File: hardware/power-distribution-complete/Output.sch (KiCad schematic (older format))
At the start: 88 parts, among them J18 POUT, J19 POUT, J20 POUT, J21 POUT, J22 POUT, J23 POUT, J24 POUT, J25 POUT, J26 POUT, J27 POUT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

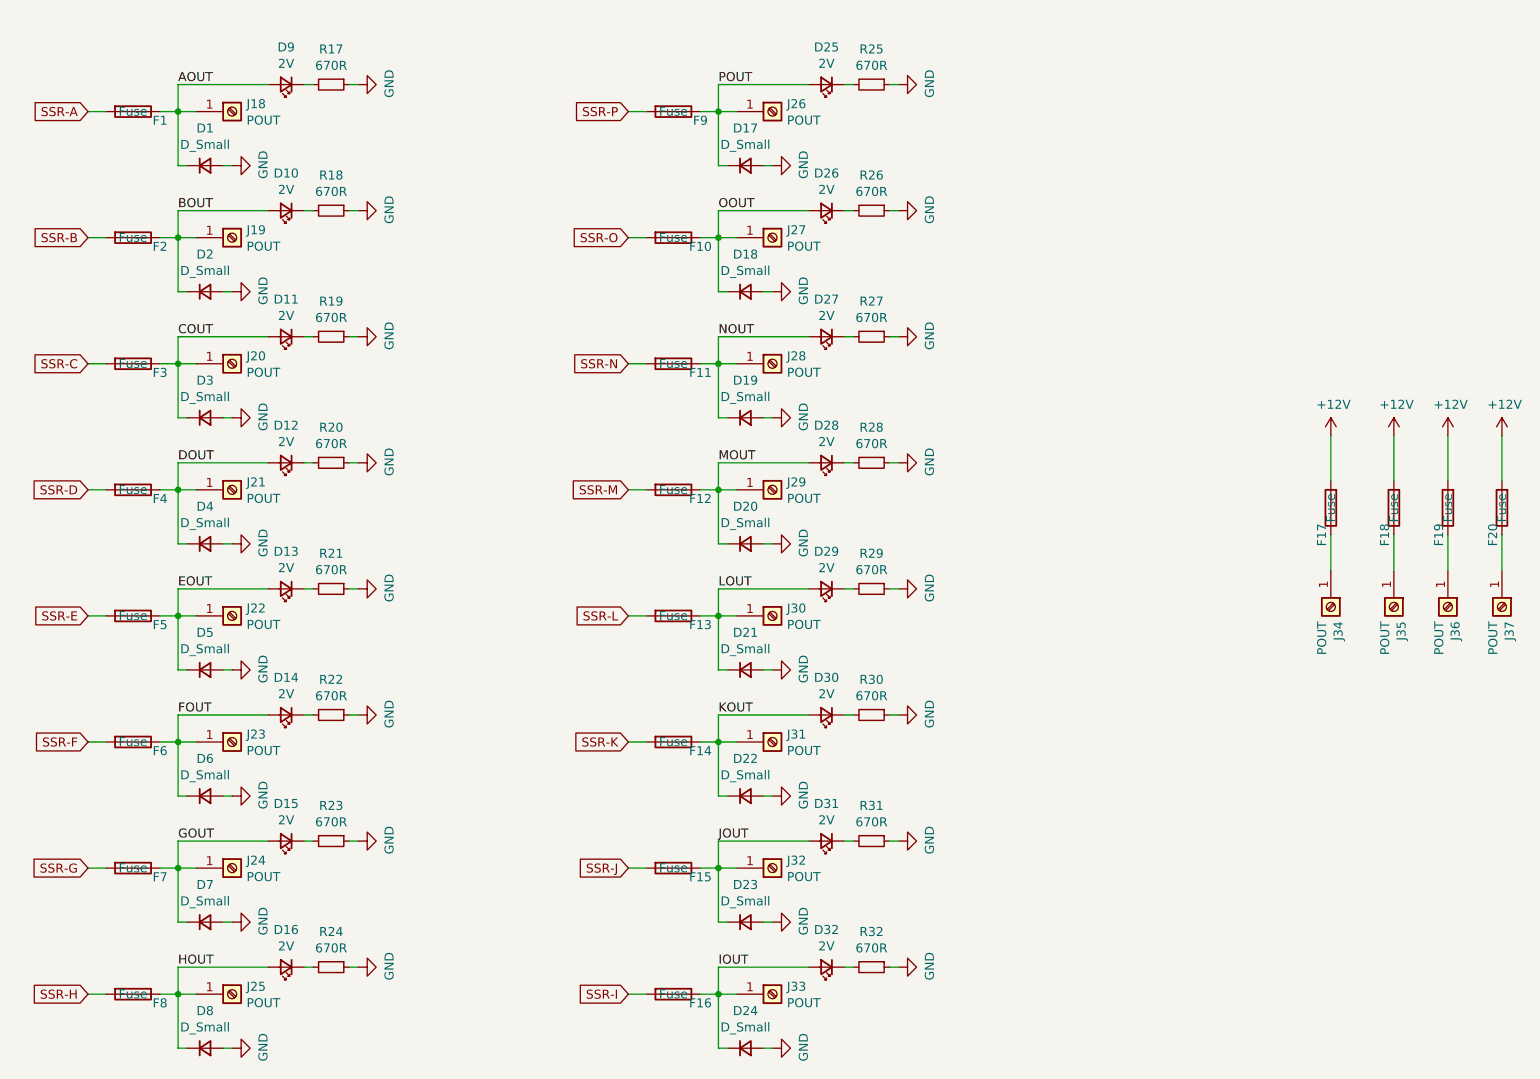
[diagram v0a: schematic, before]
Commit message: Updated the power distribution schematic and pcb
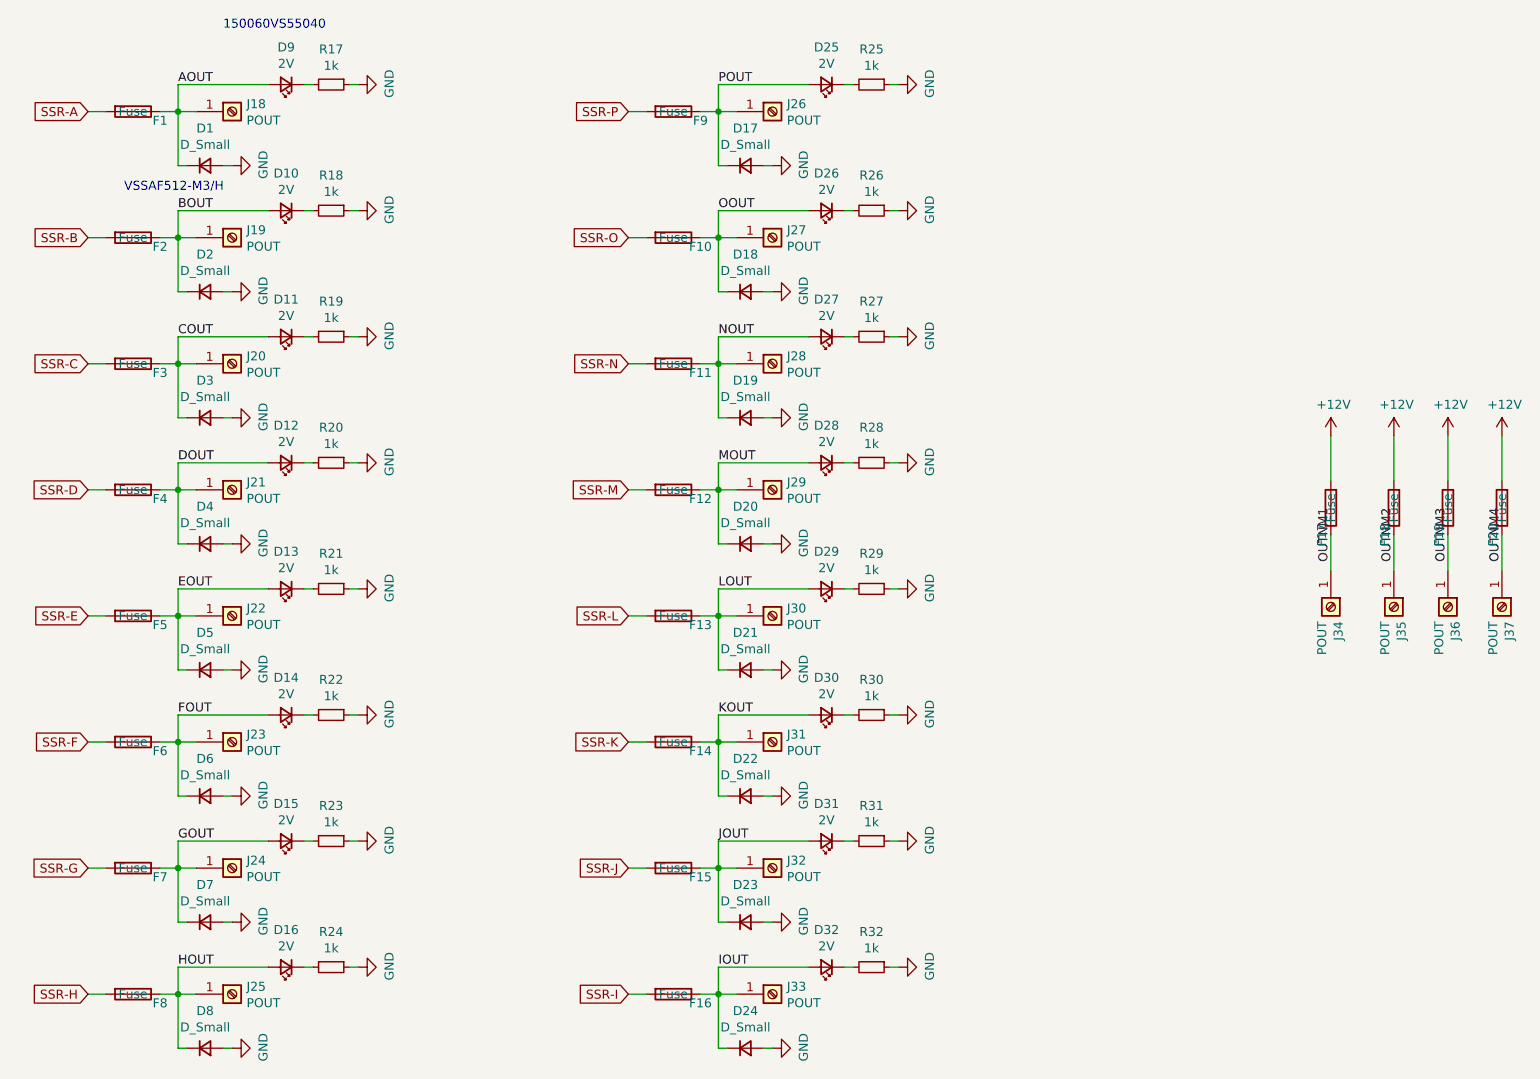
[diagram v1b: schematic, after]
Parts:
- D1, D17, D18, D19, D2, D20, D21, D22, D23, D24, D3, D4, D5, D6, D7, D8: footprint (none) -> diode:SlimSMA_DO-221AC-2
- R17, R18, R19, R20, R21, R22, R23, R24, R25, R26, R27, R28, R29, R30, R31, R32: value 670R -> 1k
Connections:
- net OUTNM1: now reaches F17.1, J34.1 (Pin_1)
- net OUTNM2: now reaches F18.1, J35.1 (Pin_1)
- net OUTNM3: now reaches F19.1, J36.1 (Pin_1)
- net OUTNM4: now reaches F20.1, J37.1 (Pin_1)
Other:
- note added: "150060VS55040"
- note added: "VSSAF512-M3/H"
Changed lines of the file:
@@
 AR Path="/5FEC946E/5FED2B12" Ref="R17"  Part="1"
 F 0 "R17" V 2654 1450 50  0000 C CNN
-F 1 "670R" V 2745 1450 50  0000 C CNN
+F 1 "1k" V 2745 1450 50  0000 C CNN
 F 2 "Resistor_SMD:R_0603_1608Metric" H 2850 1450 50  0001 C CNN
 F 3 "~" H 2850 1450 50  0001 C CNN
@@
 AR Path="/5FEC946E/5FED2B27" Ref="R18"  Part="1"
 F 0 "R18" V 2654 2150 50  0000 C CNN
-F 1 "670R" V 2745 2150 50  0000 C CNN
+F 1 "1k" V 2745 2150 50  0000 C CNN
 F 2 "Resistor_SMD:R_0603_1608Metric" H 2850 2150 50  0001 C CNN
 F 3 "~" H 2850 2150 50  0001 C CNN
@@
 AR Path="/5FEC946E/5FED2B3B" Ref="R19"  Part="1"
 F 0 "R19" V 2654 2850 50  0000 C CNN
-F 1 "670R" V 2745 2850 50  0000 C CNN
+F 1 "1k" V 2745 2850 50  0000 C CNN
 F 2 "Resistor_SMD:R_0603_1608Metric" H 2850 2850 50  0001 C CNN
 F 3 "~" H 2850 2850 50  0001 C CNN
@@
 AR Path="/5FEC946E/5FED2B4F" Ref="R20"  Part="1"
 F 0 "R20" V 2654 3550 50  0000 C CNN
-F 1 "670R" V 2745 3550 50  0000 C CNN
+F 1 "1k" V 2745 3550 50  0000 C CNN
 F 2 "Resistor_SMD:R_0603_1608Metric" H 2850 3550 50  0001 C CNN
 F 3 "~" H 2850 3550 50  0001 C CNN
@@
 AR Path="/5FEC946E/5FEE4BC2" Ref="R21"  Part="1"
 F 0 "R21" V 2654 4250 50  0000 C CNN
-F 1 "670R" V 2745 4250 50  0000 C CNN
+F 1 "1k" V 2745 4250 50  0000 C CNN
 F 2 "Resistor_SMD:R_0603_1608Metric" H 2850 4250 50  0001 C CNN
 F 3 "~" H 2850 4250 50  0001 C CNN
@@
 AR Path="/5FEC946E/5FEE4BD7" Ref="R22"  Part="1"
 F 0 "R22" V 2654 4950 50  0000 C CNN
-F 1 "670R" V 2745 4950 50  0000 C CNN
+F 1 "1k" V 2745 4950 50  0000 C CNN
 F 2 "Resistor_SMD:R_0603_1608Metric" H 2850 4950 50  0001 C CNN
 F 3 "~" H 2850 4950 50  0001 C CNN
@@
 AR Path="/5FEC946E/5FEE4BEB" Ref="R23"  Part="1"
 F 0 "R23" V 2654 5650 50  0000 C CNN
-F 1 "670R" V 2745 5650 50  0000 C CNN
+F 1 "1k" V 2745 5650 50  0000 C CNN
 F 2 "Resistor_SMD:R_0603_1608Metric" H 2850 5650 50  0001 C CNN
 F 3 "~" H 2850 5650 50  0001 C CNN
@@
 AR Path="/5FEC946E/5FEE4BFF" Ref="R24"  Part="1"
 F 0 "R24" V 2654 6350 50  0000 C CNN
-F 1 "670R" V 2745 6350 50  0000 C CNN
+F 1 "1k" V 2745 6350 50  0000 C CNN
 F 2 "Resistor_SMD:R_0603_1608Metric" H 2850 6350 50  0001 C CNN
 F 3 "~" H 2850 6350 50  0001 C CNN
@@
 AR Path="/5FEC946E/5FF051C6" Ref="R25"  Part="1"
 F 0 "R25" V 5654 1450 50  0000 C CNN
-F 1 "670R" V 5745 1450 50  0000 C CNN
+F 1 "1k" V 5745 1450 50  0000 C CNN
 F 2 "Resistor_SMD:R_0603_1608Metric" H 5850 1450 50  0001 C CNN
 F 3 "~" H 5850 1450 50  0001 C CNN
@@
 AR Path="/5FEC946E/5FF051DB" Ref="R26"  Part="1"
 F 0 "R26" V 5654 2150 50  0000 C CNN
-F 1 "670R" V 5745 2150 50  0000 C CNN
+F 1 "1k" V 5745 2150 50  0000 C CNN
 F 2 "Resistor_SMD:R_0603_1608Metric" H 5850 2150 50  0001 C CNN
 F 3 "~" H 5850 2150 50  0001 C CNN
@@
 AR Path="/5FEC946E/5FF051EF" Ref="R27"  Part="1"
 F 0 "R27" V 5654 2850 50  0000 C CNN
-F 1 "670R" V 5745 2850 50  0000 C CNN
+F 1 "1k" V 5745 2850 50  0000 C CNN
 F 2 "Resistor_SMD:R_0603_1608Metric" H 5850 2850 50  0001 C CNN
 F 3 "~" H 5850 2850 50  0001 C CNN
@@
 AR Path="/5FEC946E/5FF05203" Ref="R28"  Part="1"
 F 0 "R28" V 5654 3550 50  0000 C CNN
-F 1 "670R" V 5745 3550 50  0000 C CNN
+F 1 "1k" V 5745 3550 50  0000 C CNN
 F 2 "Resistor_SMD:R_0603_1608Metric" H 5850 3550 50  0001 C CNN
 F 3 "~" H 5850 3550 50  0001 C CNN
@@
 AR Path="/5FEC946E/5FF05266" Ref="R29"  Part="1"
 F 0 "R29" V 5654 4250 50  0000 C CNN
-F 1 "670R" V 5745 4250 50  0000 C CNN
+F 1 "1k" V 5745 4250 50  0000 C CNN
 F 2 "Resistor_SMD:R_0603_1608Metric" H 5850 4250 50  0001 C CNN
 F 3 "~" H 5850 4250 50  0001 C CNN
@@
 AR Path="/5FEC946E/5FF0527B" Ref="R30"  Part="1"
 F 0 "R30" V 5654 4950 50  0000 C CNN
-F 1 "670R" V 5745 4950 50  0000 C CNN
+F 1 "1k" V 5745 4950 50  0000 C CNN
 F 2 "Resistor_SMD:R_0603_1608Metric" H 5850 4950 50  0001 C CNN
 F 3 "~" H 5850 4950 50  0001 C CNN
@@
 AR Path="/5FEC946E/5FF0528F" Ref="R31"  Part="1"
 F 0 "R31" V 5654 5650 50  0000 C CNN
-F 1 "670R" V 5745 5650 50  0000 C CNN
+F 1 "1k" V 5745 5650 50  0000 C CNN
 F 2 "Resistor_SMD:R_0603_1608Metric" H 5850 5650 50  0001 C CNN
 F 3 "~" H 5850 5650 50  0001 C CNN
@@
 AR Path="/5FEC946E/5FF052A3" Ref="R32"  Part="1"
 F 0 "R32" V 5654 6350 50  0000 C CNN
-F 1 "670R" V 5745 6350 50  0000 C CNN
+F 1 "1k" V 5745 6350 50  0000 C CNN
 F 2 "Resistor_SMD:R_0603_1608Metric" H 5850 6350 50  0001 C CNN
 F 3 "~" H 5850 6350 50  0001 C CNN
@@
 F 0 "D1" H 2150 2107 50  0000 C CNN
 F 1 "D_Small" H 2150 2016 50  0000 C CNN
-F 2 "" V 2150 1900 50  0001 C CNN
+F 2 "diode:SlimSMA_DO-221AC-2" V 2150 1900 50  0001 C CNN
 F 3 "~" V 2150 1900 50  0001 C CNN
 	1    2150 1900
@@
 F 0 "D2" H 2150 2807 50  0000 C CNN
 F 1 "D_Small" H 2150 2716 50  0000 C CNN
-F 2 "" V 2150 2600 50  0001 C CNN
+F 2 "diode:SlimSMA_DO-221AC-2" V 2150 2600 50  0001 C CNN
 F 3 "~" V 2150 2600 50  0001 C CNN
 	1    2150 2600
@@
 F 0 "D3" H 2150 3507 50  0000 C CNN
 F 1 "D_Small" H 2150 3416 50  0000 C CNN
-F 2 "" V 2150 3300 50  0001 C CNN
+F 2 "diode:SlimSMA_DO-221AC-2" V 2150 3300 50  0001 C CNN
 F 3 "~" V 2150 3300 50  0001 C CNN
 	1    2150 3300
@@
 F 0 "D4" H 2150 4207 50  0000 C CNN
 F 1 "D_Small" H 2150 4116 50  0000 C CNN
-F 2 "" V 2150 4000 50  0001 C CNN
+F 2 "diode:SlimSMA_DO-221AC-2" V 2150 4000 50  0001 C CNN
 F 3 "~" V 2150 4000 50  0001 C CNN
 	1    2150 4000
@@
 F 0 "D5" H 2150 4907 50  0000 C CNN
 F 1 "D_Small" H 2150 4816 50  0000 C CNN
-F 2 "" V 2150 4700 50  0001 C CNN
+F 2 "diode:SlimSMA_DO-221AC-2" V 2150 4700 50  0001 C CNN
 F 3 "~" V 2150 4700 50  0001 C CNN
 	1    2150 4700
@@
 F 0 "D6" H 2150 5607 50  0000 C CNN
 F 1 "D_Small" H 2150 5516 50  0000 C CNN
-F 2 "" V 2150 5400 50  0001 C CNN
+F 2 "diode:SlimSMA_DO-221AC-2" V 2150 5400 50  0001 C CNN
 F 3 "~" V 2150 5400 50  0001 C CNN
 	1    2150 5400
@@
 F 0 "D7" H 2150 6307 50  0000 C CNN
 F 1 "D_Small" H 2150 6216 50  0000 C CNN
-F 2 "" V 2150 6100 50  0001 C CNN
+F 2 "diode:SlimSMA_DO-221AC-2" V 2150 6100 50  0001 C CNN
 F 3 "~" V 2150 6100 50  0001 C CNN
 	1    2150 6100
@@
 F 0 "D8" H 2150 7007 50  0000 C CNN
 F 1 "D_Small" H 2150 6916 50  0000 C CNN
-F 2 "" V 2150 6800 50  0001 C CNN
+F 2 "diode:SlimSMA_DO-221AC-2" V 2150 6800 50  0001 C CNN
 F 3 "~" V 2150 6800 50  0001 C CNN
 	1    2150 6800
@@
 F 0 "D24" H 5150 7007 50  0000 C CNN
 F 1 "D_Small" H 5150 6916 50  0000 C CNN
-F 2 "" V 5150 6800 50  0001 C CNN
+F 2 "diode:SlimSMA_DO-221AC-2" V 5150 6800 50  0001 C CNN
 F 3 "~" V 5150 6800 50  0001 C CNN
 	1    5150 6800
@@
 F 0 "D23" H 5150 6307 50  0000 C CNN
 F 1 "D_Small" H 5150 6216 50  0000 C CNN
-F 2 "" V 5150 6100 50  0001 C CNN
+F 2 "diode:SlimSMA_DO-221AC-2" V 5150 6100 50  0001 C CNN
 F 3 "~" V 5150 6100 50  0001 C CNN
 	1    5150 6100
@@
 F 0 "D22" H 5150 5607 50  0000 C CNN
 F 1 "D_Small" H 5150 5516 50  0000 C CNN
-F 2 "" V 5150 5400 50  0001 C CNN
+F 2 "diode:SlimSMA_DO-221AC-2" V 5150 5400 50  0001 C CNN
 F 3 "~" V 5150 5400 50  0001 C CNN
 	1    5150 5400
@@
 F 0 "D21" H 5150 4907 50  0000 C CNN
 F 1 "D_Small" H 5150 4816 50  0000 C CNN
-F 2 "" V 5150 4700 50  0001 C CNN
+F 2 "diode:SlimSMA_DO-221AC-2" V 5150 4700 50  0001 C CNN
 F 3 "~" V 5150 4700 50  0001 C CNN
 	1    5150 4700
@@
 F 0 "D20" H 5150 4207 50  0000 C CNN
 F 1 "D_Small" H 5150 4116 50  0000 C CNN
-F 2 "" V 5150 4000 50  0001 C CNN
+F 2 "diode:SlimSMA_DO-221AC-2" V 5150 4000 50  0001 C CNN
 F 3 "~" V 5150 4000 50  0001 C CNN
 	1    5150 4000
@@
 F 0 "D19" H 5150 3507 50  0000 C CNN
 F 1 "D_Small" H 5150 3416 50  0000 C CNN
-F 2 "" V 5150 3300 50  0001 C CNN
+F 2 "diode:SlimSMA_DO-221AC-2" V 5150 3300 50  0001 C CNN
 F 3 "~" V 5150 3300 50  0001 C CNN
 	1    5150 3300
@@
 F 0 "D18" H 5150 2807 50  0000 C CNN
 F 1 "D_Small" H 5150 2716 50  0000 C CNN
-F 2 "" V 5150 2600 50  0001 C CNN
+F 2 "diode:SlimSMA_DO-221AC-2" V 5150 2600 50  0001 C CNN
 F 3 "~" V 5150 2600 50  0001 C CNN
 	1    5150 2600
@@
 F 0 "D17" H 5150 2107 50  0000 C CNN
 F 1 "D_Small" H 5150 2016 50  0000 C CNN
-F 2 "" V 5150 1900 50  0001 C CNN
+F 2 "diode:SlimSMA_DO-221AC-2" V 5150 1900 50  0001 C CNN
 F 3 "~" V 5150 1900 50  0001 C CNN
 	1    5150 1900
@@
 Wire Wire Line
 	5300 1900 5250 1900
+Text Notes 1700 2050 0    50   ~ 0
+VSSAF512-M3/H
+Text Label 8400 4100 1    50   ~ 0
+OUTNM1
+Text Label 8750 4100 1    50   ~ 0
+OUTNM2
+Text Label 9050 4100 1    50   ~ 0
+OUTNM3
+Text Label 9350 4100 1    50   ~ 0
+OUTNM4
+Text Notes 2250 1150 0    50   ~ 0
+150060VS55040
 $EndSCHEMATC
